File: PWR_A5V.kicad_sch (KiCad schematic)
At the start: 7 parts, among them Q4 STS5DNF60L

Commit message: possible working power mux
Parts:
- removed D11, D12: B340, Diode_SMD:D_SMC, symbol Diode:B340
- removed Q4: STS5DNF60L, SOIC127P600X175-8N, symbol 0_SamacSys_Parts:STS5DNF60L
- removed R44, R45: 33R, Resistor_SMD:R_0603_1608Metric_Pad0.98x0.95mm_HandSolder, symbol Device:R
- removed R50, R51: 10k, symbol Device:R
- added C42, C46: 1uF, Capacitor_SMD:C_0603_1608Metric_Pad1.08x0.95mm_HandSolder, symbol Device:C
- added IC3: LP2951-50DRG4, SOIC127P600X175-8N, symbol 0_SamacSys_Parts:LP2951-50DRG4
- added R13: 100k, Resistor_SMD:R_0603_1608Metric_Pad0.98x0.95mm_HandSolder, symbol Device:R
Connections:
- net 12V: now also C46.1, IC3.8 (INPUT)
- net GND: now also C46.2
- new net: IC3.6 (VTAP), IC3.7 (FEEDBACK)
- new net 3V3: R13.2
- new net A5V: C42.1, IC3.1 (OUTPUT), IC3.2 (SENSE)
- new net A5V_PG: IC3.5 (~{ERROR}), R13.1
- new net AGND: C42.2, IC3.3 (SHUTDOWN), IC3.4 (GND)

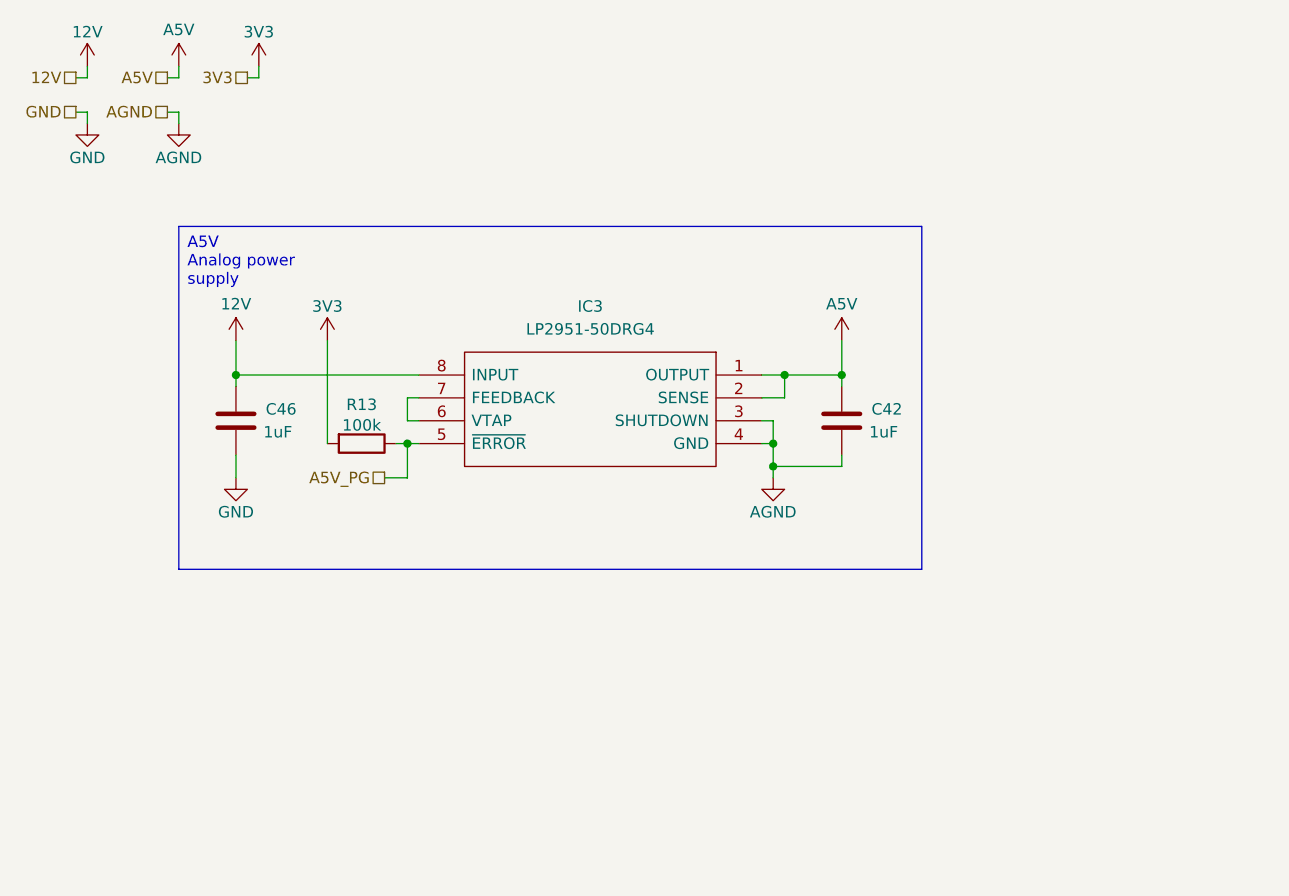
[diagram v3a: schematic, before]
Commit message: finished initial esp routing
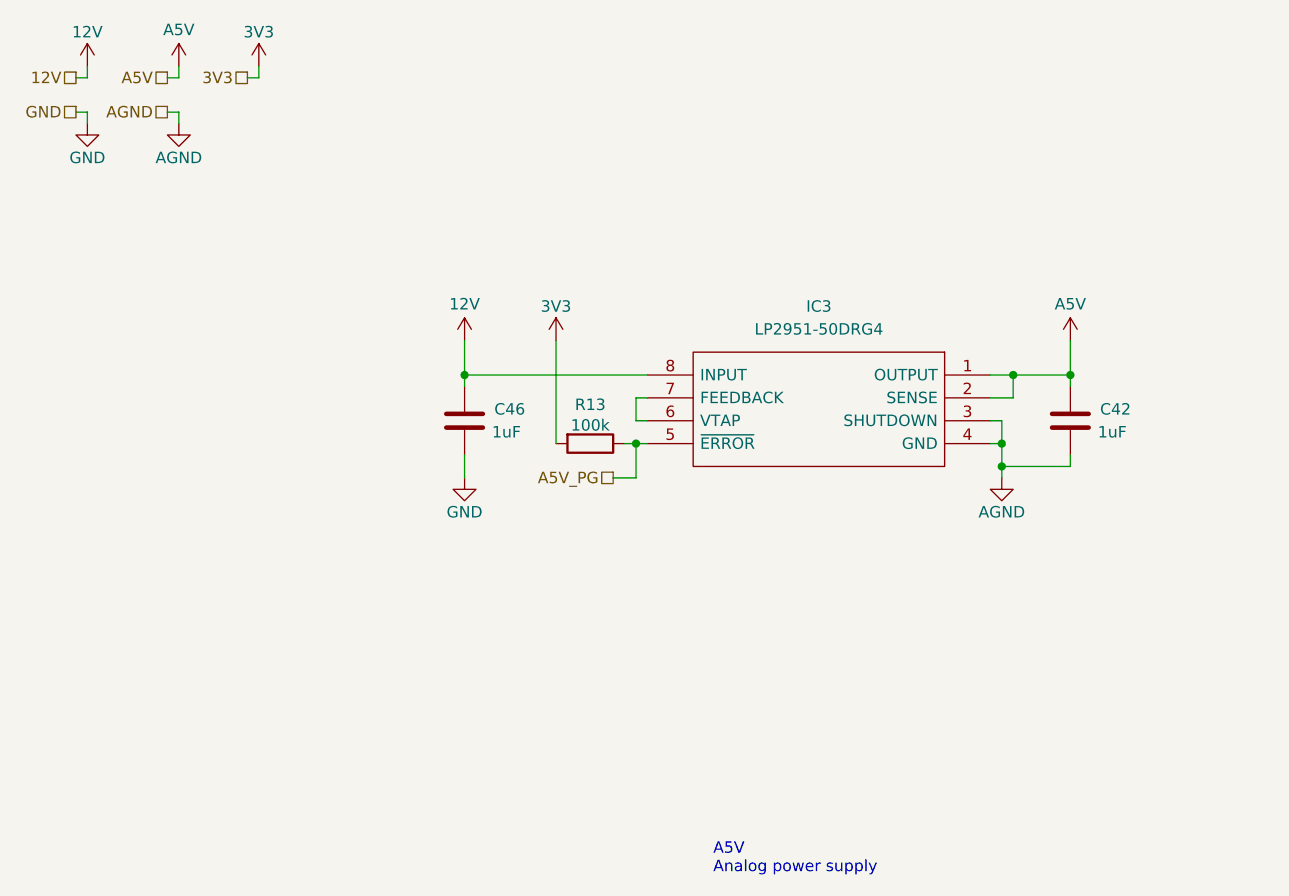
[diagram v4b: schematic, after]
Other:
- moved on the sheet: C42, C46, IC3, R13

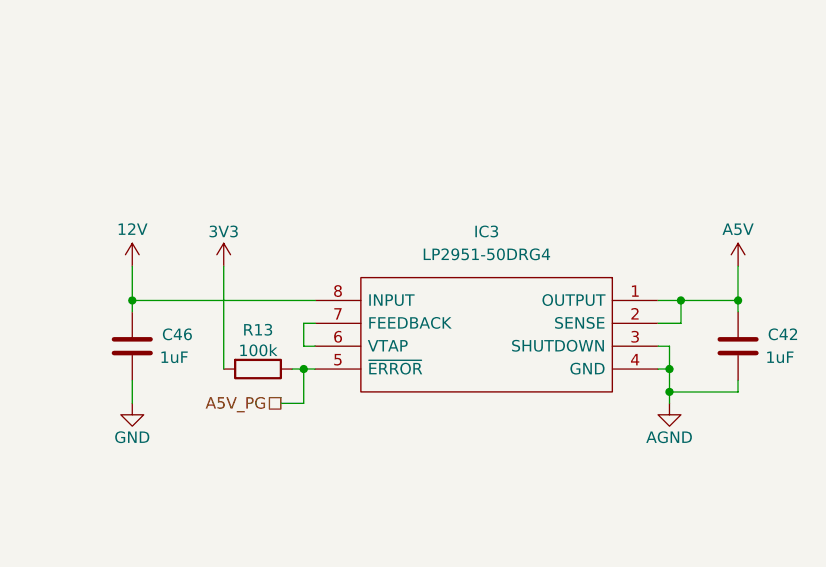
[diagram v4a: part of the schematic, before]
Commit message: redid annotations, added test point
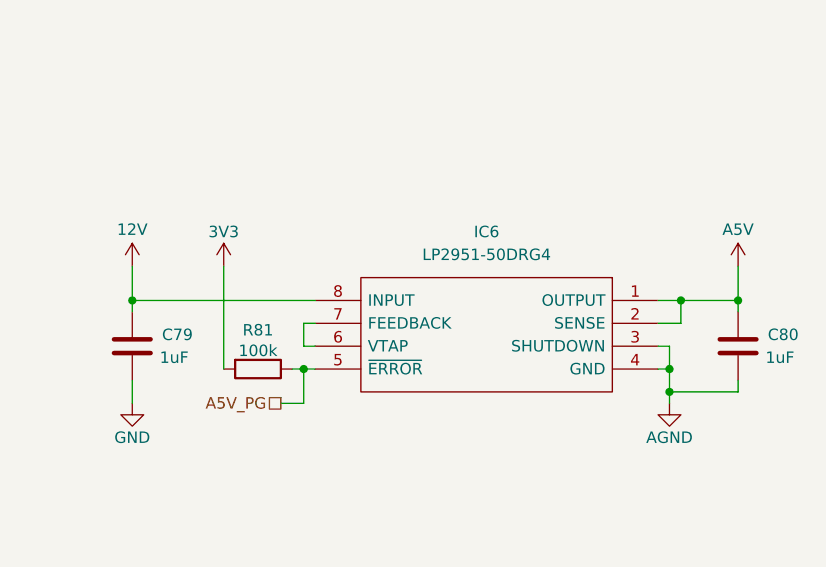
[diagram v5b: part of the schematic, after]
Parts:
- renumbered C46 to C79, C42 to C80, IC3 to IC6, R13 to R81
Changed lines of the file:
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@@
 		(on_board yes)
 		(dnp no)
-		(property "Reference" "IC3"
+		(property "Reference" "IC6"
 			(at 102.87 45.72 0)
 			(effects
@@
 			(project "NCU"
 				(path "/3aee14c3-5480-4f7c-989e-3fef81779034/05e3be97-98f6-4518-a1a7-240d4da327e6/bd2125f3-b038-4fbf-8844-7722167ed0b9"
-					(reference "IC3")
+					(reference "IC6")
 					(unit 1)
 				)
@@
 		(on_board yes)
 		(dnp no)
-		(property "Reference" "#PWR0275"
+		(property "Reference" "#PWR0284"
 			(at 21.59 22.86 0)
 			(effects
@@
 			(project "NCU"
 				(path "/3aee14c3-5480-4f7c-989e-3fef81779034/05e3be97-98f6-4518-a1a7-240d4da327e6/bd2125f3-b038-4fbf-8844-7722167ed0b9"
-					(reference "#PWR0275")
+					(reference "#PWR0284")
 					(unit 1)
 				)
@@
 		(on_board yes)
 		(dnp no)
-		(property "Reference" "#PWR064"
+		(property "Reference" "#PWR0289"
 			(at 63.5 53.34 0)
 			(effects
@@
 			(project "NCU"
 				(path "/3aee14c3-5480-4f7c-989e-3fef81779034/05e3be97-98f6-4518-a1a7-240d4da327e6/bd2125f3-b038-4fbf-8844-7722167ed0b9"
-					(reference "#PWR064")
+					(reference "#PWR0289")
 					(unit 1)
 				)
@@
 		(on_board yes)
 		(dnp no)
-		(property "Reference" "#PWR0155"
+		(property "Reference" "#PWR0291"
 			(at 73.66 53.34 0)
 			(effects
@@
 			(project "NCU"
 				(path "/3aee14c3-5480-4f7c-989e-3fef81779034/05e3be97-98f6-4518-a1a7-240d4da327e6/bd2125f3-b038-4fbf-8844-7722167ed0b9"
-					(reference "#PWR0155")
+					(reference "#PWR0291")
 					(unit 1)
 				)
@@
 		(on_board yes)
 		(dnp no)
-		(property "Reference" "C42"
+		(property "Reference" "C80"
 			(at 134.112 57.15 0)
 			(effects
@@
 			(project "NCU"
 				(path "/3aee14c3-5480-4f7c-989e-3fef81779034/05e3be97-98f6-4518-a1a7-240d4da327e6/bd2125f3-b038-4fbf-8844-7722167ed0b9"
-					(reference "C42")
+					(reference "C80")
 					(unit 1)
 				)
@@
 		(on_board yes)
 		(dnp no)
-		(property "Reference" "R13"
+		(property "Reference" "R81"
 			(at 77.47 56.642 90)
 			(effects
@@
 			(project "NCU"
 				(path "/3aee14c3-5480-4f7c-989e-3fef81779034/05e3be97-98f6-4518-a1a7-240d4da327e6/bd2125f3-b038-4fbf-8844-7722167ed0b9"
-					(reference "R13")
+					(reference "R81")
 					(unit 1)
 				)
@@
 		(on_board yes)
 		(dnp no)
-		(property "Reference" "#PWR0278"
+		(property "Reference" "#PWR0287"
 			(at 31.75 31.75 0)
 			(effects
@@
 			(project "NCU"
 				(path "/3aee14c3-5480-4f7c-989e-3fef81779034/05e3be97-98f6-4518-a1a7-240d4da327e6/bd2125f3-b038-4fbf-8844-7722167ed0b9"
-					(reference "#PWR0278")
+					(reference "#PWR0287")
 					(unit 1)
 				)
@@
 		(on_board yes)
 		(dnp no)
-		(property "Reference" "#PWR081"
+		(property "Reference" "#PWR0290"
 			(at 63.5 71.12 0)
 			(effects
@@
 			(project "NCU"
 				(path "/3aee14c3-5480-4f7c-989e-3fef81779034/05e3be97-98f6-4518-a1a7-240d4da327e6/bd2125f3-b038-4fbf-8844-7722167ed0b9"
-					(reference "#PWR081")
+					(reference "#PWR0290")
 					(unit 1)
 				)
@@
 		(on_board yes)
 		(dnp no)
-		(property "Reference" "#PWR075"
+		(property "Reference" "#PWR0292"
 			(at 123.19 71.12 0)
 			(effects
@@
 			(project "NCU"
 				(path "/3aee14c3-5480-4f7c-989e-3fef81779034/05e3be97-98f6-4518-a1a7-240d4da327e6/bd2125f3-b038-4fbf-8844-7722167ed0b9"
-					(reference "#PWR075")
+					(reference "#PWR0292")
 					(unit 1)
 				)
@@
 		(on_board yes)
 		(dnp no)
-		(property "Reference" "#PWR0264"
+		(property "Reference" "#PWR0288"
 			(at 40.64 22.86 0)
 			(effects
@@
 			(project "NCU"
 				(path "/3aee14c3-5480-4f7c-989e-3fef81779034/05e3be97-98f6-4518-a1a7-240d4da327e6/bd2125f3-b038-4fbf-8844-7722167ed0b9"
-					(reference "#PWR0264")
+					(reference "#PWR0288")
 					(unit 1)
 				)
@@
 		(on_board yes)
 		(dnp no)
-		(property "Reference" "#PWR0281"
+		(property "Reference" "#PWR0286"
 			(at 31.75 22.86 0)
 			(effects
@@
 			(project "NCU"
 				(path "/3aee14c3-5480-4f7c-989e-3fef81779034/05e3be97-98f6-4518-a1a7-240d4da327e6/bd2125f3-b038-4fbf-8844-7722167ed0b9"
-					(reference "#PWR0281")
+					(reference "#PWR0286")
 					(unit 1)
 				)
@@
 		(on_board yes)
 		(dnp no)
-		(property "Reference" "#PWR0276"
+		(property "Reference" "#PWR0285"
 			(at 21.59 31.75 0)
 			(effects
@@
 			(project "NCU"
 				(path "/3aee14c3-5480-4f7c-989e-3fef81779034/05e3be97-98f6-4518-a1a7-240d4da327e6/bd2125f3-b038-4fbf-8844-7722167ed0b9"
-					(reference "#PWR0276")
+					(reference "#PWR0285")
 					(unit 1)
 				)
@@
 		(on_board yes)
 		(dnp no)
-		(property "Reference" "#PWR073"
+		(property "Reference" "#PWR0293"
 			(at 130.81 53.34 0)
 			(effects
@@
 			(project "NCU"
 				(path "/3aee14c3-5480-4f7c-989e-3fef81779034/05e3be97-98f6-4518-a1a7-240d4da327e6/bd2125f3-b038-4fbf-8844-7722167ed0b9"
-					(reference "#PWR073")
+					(reference "#PWR0293")
 					(unit 1)
 				)
@@
 		(on_board yes)
 		(dnp no)
-		(property "Reference" "C46"
+		(property "Reference" "C79"
 			(at 66.802 57.15 0)
 			(effects
@@
 			(project "NCU"
 				(path "/3aee14c3-5480-4f7c-989e-3fef81779034/05e3be97-98f6-4518-a1a7-240d4da327e6/bd2125f3-b038-4fbf-8844-7722167ed0b9"
-					(reference "C46")
-					(unit 1)
-				)
+					(reference "C79")
+					(unit 1)
+				)
